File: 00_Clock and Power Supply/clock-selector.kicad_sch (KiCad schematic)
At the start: 6 parts, among them U5 74LS01, U6 74LS01

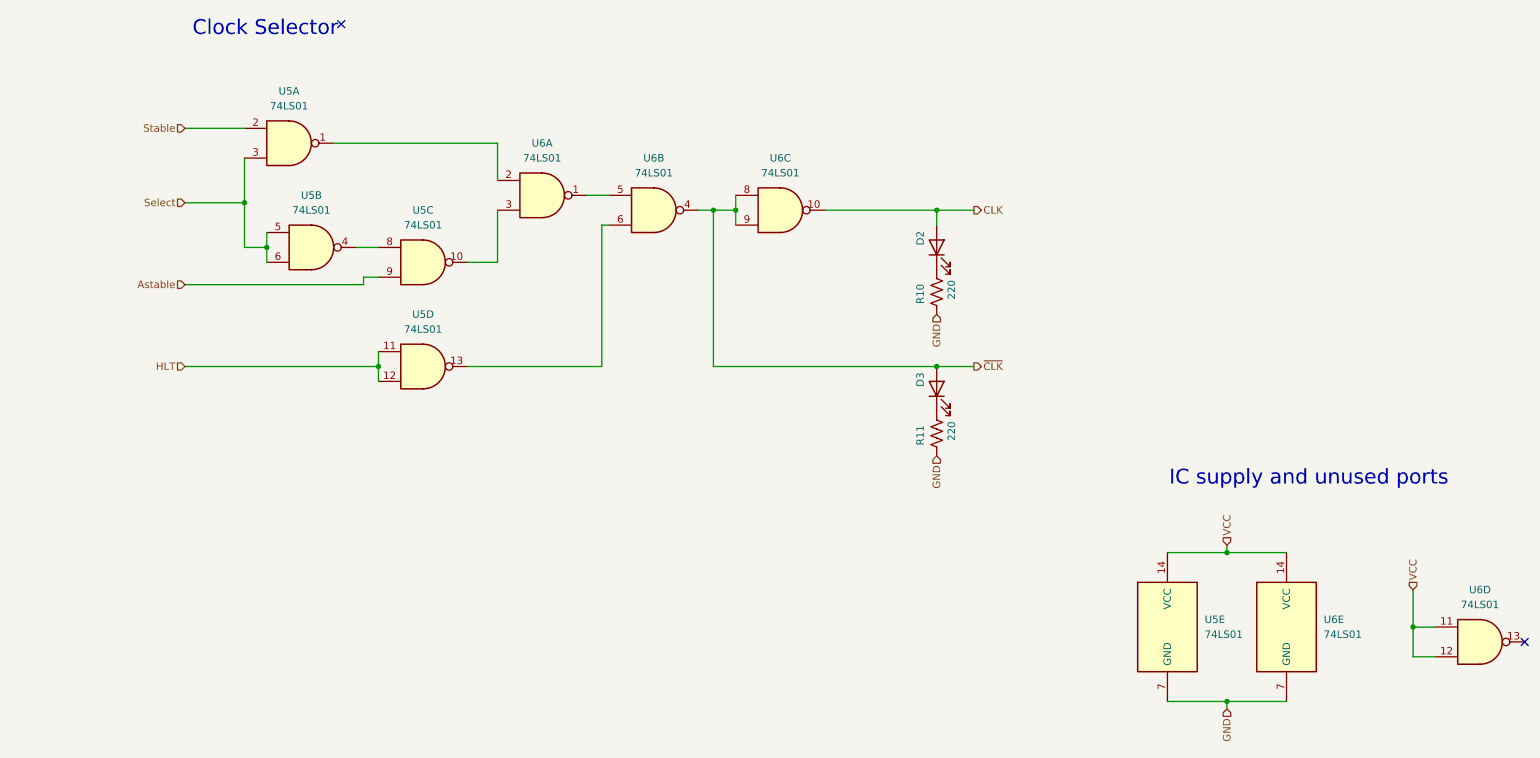
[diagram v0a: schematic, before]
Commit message: Last revision of the cpu, all boards have been ordered. Implementation to be tested and documented in following commits.
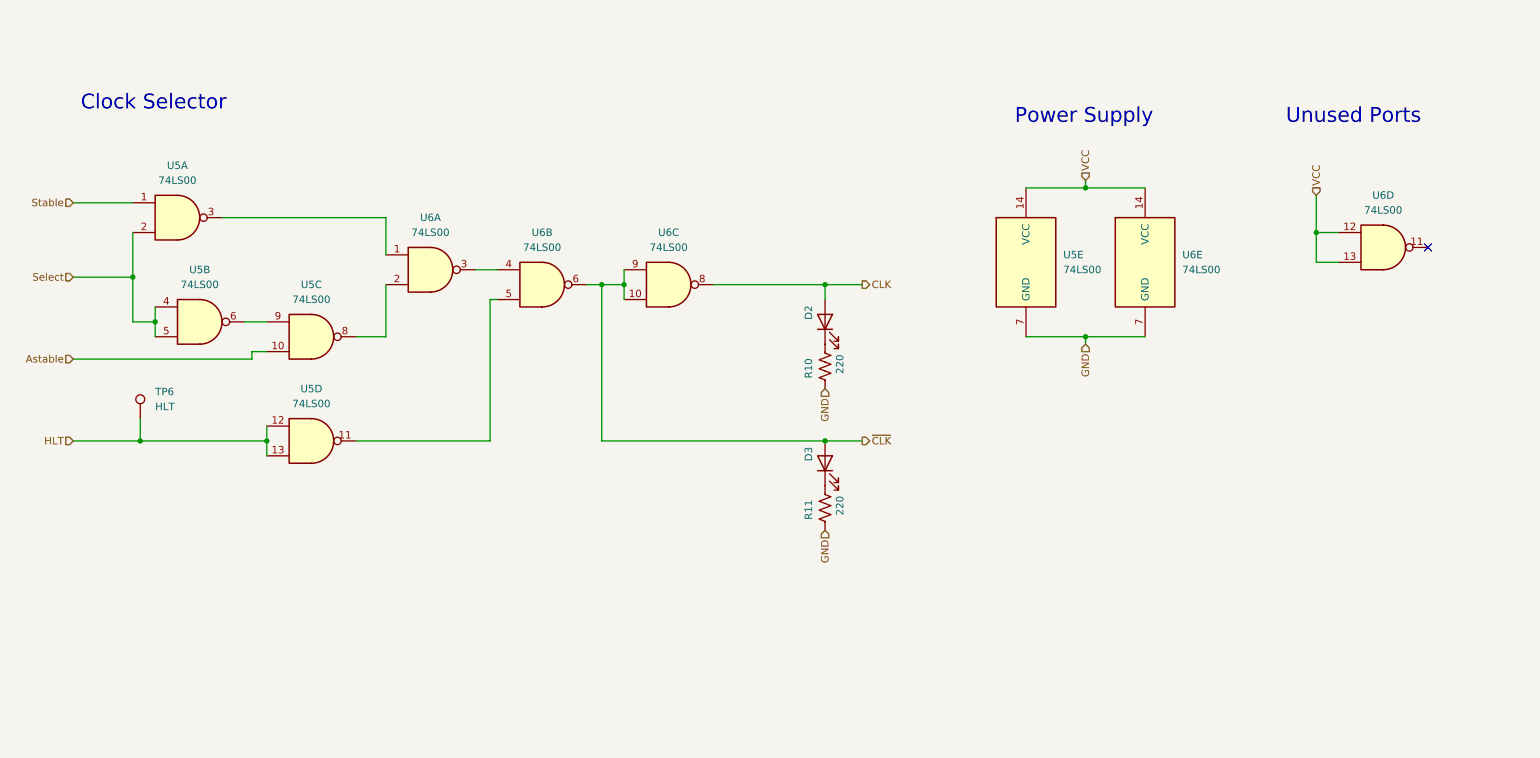
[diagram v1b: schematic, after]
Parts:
- removed U5, U6: 74LS01, Package_DIP:DIP-14_W7.62mm, symbol 74xx:74LS01
- added TP6: HLT, TestPoint:TestPoint_Loop_D3.50mm_Drill0.9mm_Beaded, symbol Connector:TestPoint
- added U5, U6: 74LS00, Package_DIP:DIP-14_W7.62mm, symbol 74xx:74LS00
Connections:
- net Astable: now also U5.10
- net CLK: now also U6.8
- net GND: now also U5.7 (GND), U6.7 (GND)
- net HLT: now also TP6.1, U5.12, U5.13
- net Select: now also U5.2, U5.4, U5.5
- net Stable: now also U5.1
- net VCC: now also U5.14 (VCC), U6.12, U6.13, U6.14 (VCC)
- net ~{CLK}: now also U6.10, U6.6, U6.9
- new net: U5.8, U6.2
- new net: U5.6, U5.9
- new net: U5.3, U6.1
- new net: U5.11, U6.5
- new net: U6.3, U6.4
- no-connect marks 2 -> 1
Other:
- note added: "Power Supply"
- note added: "Unused Ports"
- note removed: "IC supply and unused ports"
- moved on the sheet: D2, D3, R10, R11
